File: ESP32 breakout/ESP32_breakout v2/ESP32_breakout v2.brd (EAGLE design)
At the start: 33 parts, among them U1 ESP-WROOM-32, U2 NCP-1117, Y1 12MHz

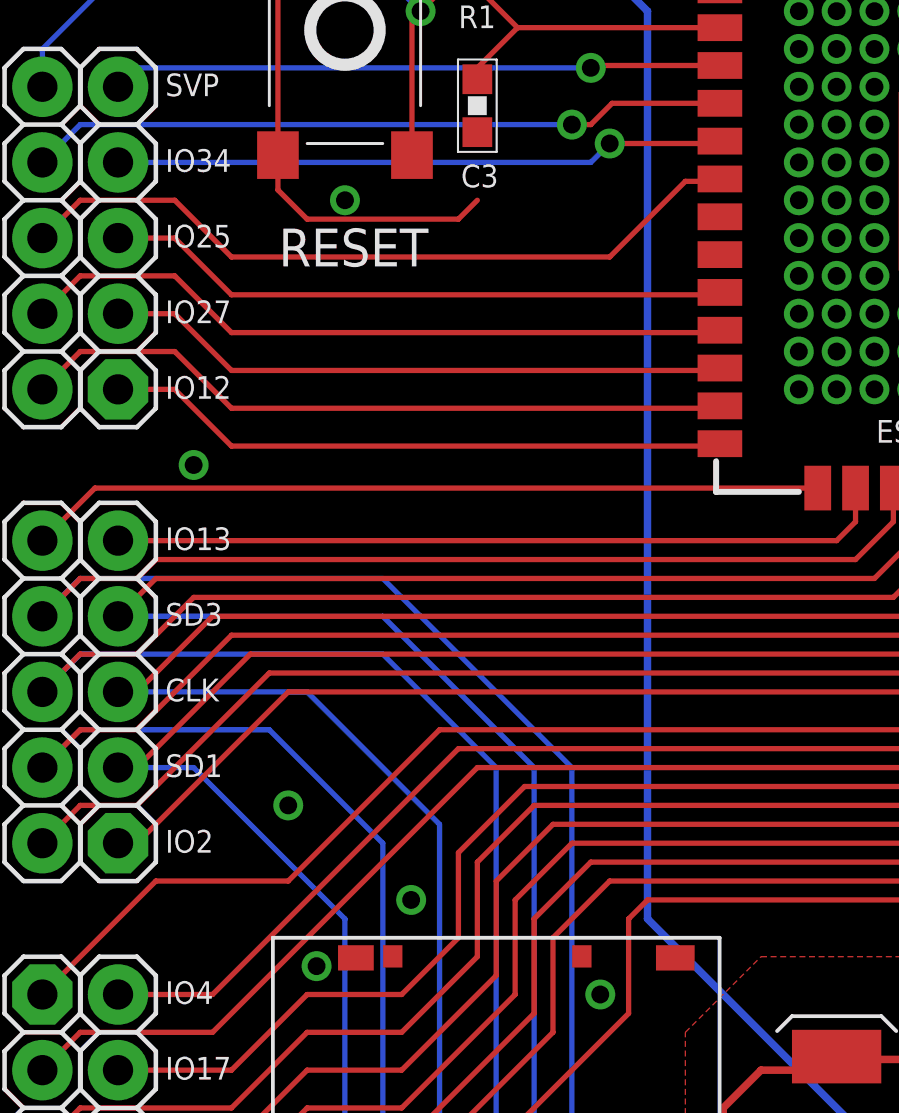
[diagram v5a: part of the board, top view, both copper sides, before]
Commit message: More vias
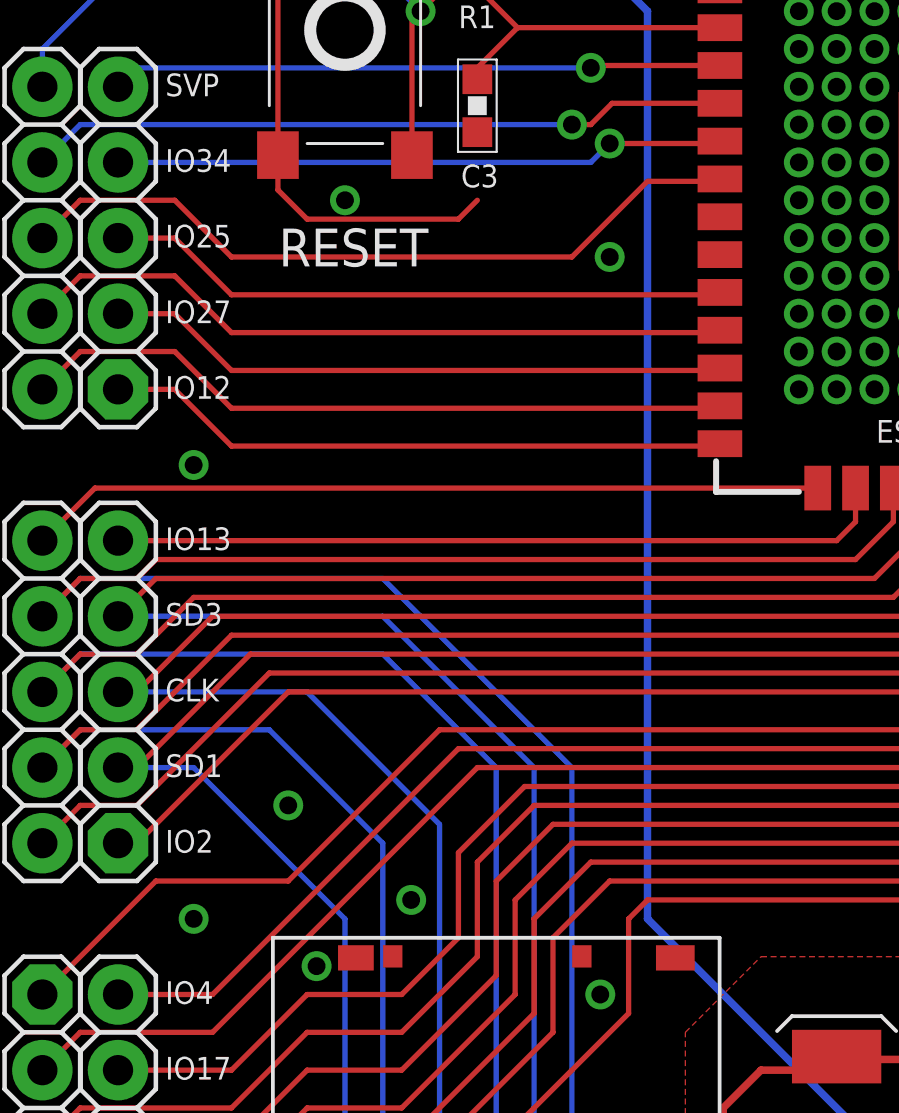
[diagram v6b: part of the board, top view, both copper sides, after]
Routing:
- net GND: vias 102 -> 104
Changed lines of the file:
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@@
 <text x="54.9275" y="42.545" size="1.27" layer="21" font="vector" ratio="20">BOOT</text>
 <text x="56.515" y="27.305" size="0.762" layer="21" font="vector" ratio="20">U1</text>
+<dimension x1="-2.54" y1="55.88" x2="-2.54" y2="-2.54" x3="-3.81" y3="26.67" textsize="1.778" layer="48" unit="inch" visible="yes"/>
+<dimension x1="0" y1="2.54" x2="69.85" y2="2.54" x3="34.925" y3="-6.35" textsize="1.778" layer="48" unit="inch" visible="yes"/>
+<dimension x1="-6.35" y1="55.88" x2="-6.35" y2="-2.54" x3="-7.62" y3="26.67" textsize="1.778" layer="48" visible="yes"/>
+<dimension x1="0" y1="-1.27" x2="69.85" y2="-1.27" x3="34.925" y3="-10.16" textsize="1.778" layer="48" visible="yes"/>
 </plain>
 <attributes>
@@
 <via x="54.61" y="35.56" extent="1-16" drill="0.6"/>
 <via x="22.5425" y="17.78" extent="1-16" drill="0.6"/>
+<via x="22.86" y="42.545" extent="1-16" drill="0.6"/>
+<via x="8.89" y="20.32" extent="1-16" drill="0.6"/>
 </signal>
 <signal name="+3V3">
@@
 <wire x1="5.08" y1="44.45" x2="8.255" y2="44.45" width="0.1778" layer="1"/>
 <wire x1="8.255" y1="44.45" x2="10.16" y2="42.545" width="0.1778" layer="1"/>
-<wire x1="10.16" y1="42.545" x2="22.86" y2="42.545" width="0.1778" layer="1"/>
-<wire x1="22.86" y1="42.545" x2="25.4" y2="45.085" width="0.1778" layer="1"/>
-<wire x1="25.4" y1="45.085" x2="26.48" y2="45.085" width="0.1778" layer="1"/>
+<wire x1="10.16" y1="42.545" x2="21.59" y2="42.545" width="0.1778" layer="1"/>
+<wire x1="21.59" y1="42.545" x2="24.13" y2="45.085" width="0.1778" layer="1"/>
+<wire x1="24.13" y1="45.085" x2="26.48" y2="45.085" width="0.1778" layer="1"/>
 <wire x1="26.48" y1="45.085" x2="26.56" y2="45.165" width="0.1778" layer="1"/>
 </signal>
